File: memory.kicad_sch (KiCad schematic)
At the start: 0 parts

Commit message: Gathering memory components
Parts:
- added IC5: S70KL1282GABHV020, BGA24C100P5X5_600X800X100, symbol SamacSys_Parts:S70KL1282GABHV020
- added IC6: MT25QU02GCBB8E12-0AAT, BGA24C100P5X5_600X800X120, symbol SamacSys_Parts:MT25QU02GCBB8E12-0AAT
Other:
- note added: "HyperRAM (Fast DRAM)"
- note added: "NOR FLASH"
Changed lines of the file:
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@@
 (kicad_sch (version 20230121) (generator eeschema)
-  (paper "A4")
+  (paper "A5")
   (title_block
     (title "Memory")
   )
+  (text "HyperRAM (Fast DRAM)" (at 57.15 62.23 0)
+    (effects (font (size 1.27 1.27)) (justify left bottom))
+  )
+  (text "NOR FLASH" (at 140.97 77.47 0)
+    (effects (font (size 1.27 1.27)) (justify left bottom))
+  )
+  (symbol (lib_id "SamacSys_Parts:MT25QU02GCBB8E12-0AAT") (at 127 44.45 0) (unit 1)
+    (in_bom yes) (on_board yes) (dnp no) (fields_autoplaced)
+    (property "Reference" "IC6" (at 146.05 36.83 0)
+      (effects (font (size 1.27 1.27)))
+    )
+    (property "Value" "MT25QU02GCBB8E12-0AAT" (at 146.05 39.37 0)
+      (effects (font (size 1.27 1.27)))
+    )
+    (property "Footprint" "BGA24C100P5X5_600X800X120" (at 161.29 139.37 0)
+      (effects (font (size 1.27 1.27)) (justify left top) hide)
+    )
+    (property "Datasheet" "https://datasheet.datasheetarchive.com/originals/distributors/DKDS42/DSANUWW0045439.pdf" (at 161.29 239.37 0)
+      (effects (font (size 1.27 1.27)) (justify left top) hide)
+    )
+    (property "Height" "1.2" (at 161.29 439.37 0)
+      (effects (font (size 1.27 1.27)) (justify left top) hide)
+    )
+    (property "Mouser Part Number" "340-336522-TRAY" (at 161.29 539.37 0)
+      (effects (font (size 1.27 1.27)) (justify left top) hide)
+    )
+    (property "Mouser Price/Stock" "https://www.mouser.co.uk/ProductDetail/Micron/MT25QU02GCBB8E12-0AAT?qs=rrS6PyfT74d7p8mPaOod1Q%3D%3D" (at 161.29 639.37 0)
+      (effects (font (size 1.27 1.27)) (justify left top) hide)
+    )
+    (property "Manufacturer_Name" "Micron" (at 161.29 739.37 0)
+      (effects (font (size 1.27 1.27)) (justify left top) hide)
+    )
+    (property "Manufacturer_Part_Number" "MT25QU02GCBB8E12-0AAT" (at 161.29 839.37 0)
+      (effects (font (size 1.27 1.27)) (justify left top) hide)
+    )
+    (pin "E3")
+    (pin "C3")
+    (pin "B1")
+    (pin "C4")
+    (pin "C5")
+    (pin "D5")
+    (pin "B4")
+    (pin "B3")
+    (pin "E5")
+    (pin "E2")
+    (pin "A4")
+    (pin "D2")
+    (pin "B5")
+    (pin "A5")
+    (pin "A3")
+    (pin "B2")
+    (pin "D3")
+    (pin "E4")
+    (pin "C1")
+    (pin "C2")
+    (pin "D1")
+    (pin "A2")
+    (pin "E1")
+    (pin "D4")
+    (instances
+      (project "drone"
+        (path "/d34d8324-c983-4098-8d7e-5c2fbd34794d/4100cf90-4d91-4a61-8724-d501936d5e21"
+          (reference "IC6") (unit 1)
+        )
+      )
+    )
+  )
+  (symbol (lib_id "SamacSys_Parts:S70KL1282GABHV020") (at 50.8 29.21 0) (unit 1)
+    (in_bom yes) (on_board yes) (dnp no) (fields_autoplaced)
+    (property "Reference" "IC5" (at 67.31 21.59 0)
+      (effects (font (size 1.27 1.27)))
+    )
+    (property "Value" "S70KL1282GABHV020" (at 67.31 24.13 0)
+      (effects (font (size 1.27 1.27)))
+    )
+    (property "Footprint" "BGA24C100P5X5_600X800X100" (at 80.01 124.13 0)
+      (effects (font (size 1.27 1.27)) (justify left top) hide)
+    )
+    (property "Datasheet" "https://www.cypress.com/file/501841/download" (at 80.01 224.13 0)
+      (effects (font (size 1.27 1.27)) (justify left top) hide)
+    )
+    (property "Height" "1" (at 80.01 424.13 0)
+      (effects (font (size 1.27 1.27)) (justify left top) hide)
+    )
+    (property "Mouser Part Number" "727-S70KL1282GABHV2" (at 80.01 524.13 0)
+      (effects (font (size 1.27 1.27)) (justify left top) hide)
+    )
+    (property "Mouser Price/Stock" "https://www.mouser.co.uk/ProductDetail/Infineon-Technologies/S70KL1282GABHV020?qs=sPbYRqrBIVnZUdfTED8OOQ%3D%3D" (at 80.01 624.13 0)
+      (effects (font (size 1.27 1.27)) (justify left top) hide)
+    )
+    (property "Manufacturer_Name" "Infineon" (at 80.01 724.13 0)
+      (effects (font (size 1.27 1.27)) (justify left top) hide)
+    )
+    (property "Manufacturer_Part_Number" "S70KL1282GABHV020" (at 80.01 824.13 0)
+      (effects (font (size 1.27 1.27)) (justify left top) hide)
+    )
+    (pin "E4")
+    (pin "B5")
+    (pin "A2")
+    (pin "C5")
+    (pin "E5")
+    (pin "E2")
+    (pin "C2")
+    (pin "D2")
+    (pin "A5")
+    (pin "E1")
+    (pin "D5")
+    (pin "B3")
+    (pin "D3")
+    (pin "B4")
+    (pin "C4")
+    (pin "B2")
+    (pin "D1")
+    (pin "C1")
+    (pin "C3")
+    (pin "A4")
+    (pin "E3")
+    (pin "A3")
+    (pin "B1")
+    (pin "D4")
+    (instances
+      (project "drone"
+        (path "/d34d8324-c983-4098-8d7e-5c2fbd34794d/4100cf90-4d91-4a61-8724-d501936d5e21"
+          (reference "IC5") (unit 1)
+        )
+      )
+    )
+  )
 )

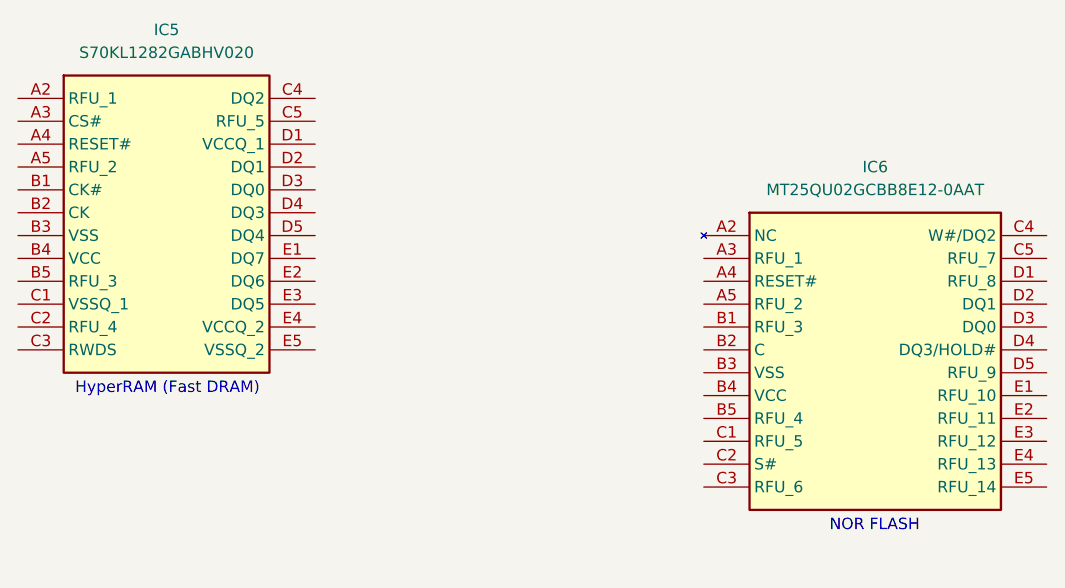
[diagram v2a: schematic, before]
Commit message: Exchanged flash for same one as on the gatemate dev board
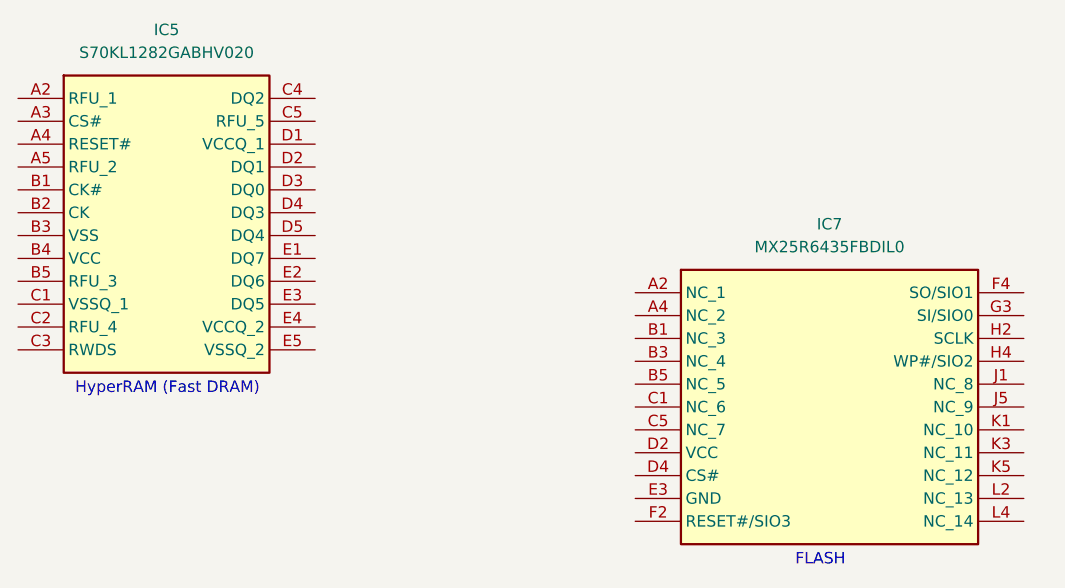
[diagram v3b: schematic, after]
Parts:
- removed IC6: MT25QU02GCBB8E12-0AAT, BGA24C100P5X5_600X800X120, symbol SamacSys_Parts:MT25QU02GCBB8E12-0AAT
- added IC7: MX25R6435FBDIL0, MX25R6435FBDIL0, symbol SamacSys_Parts:MX25R6435FBDIL0
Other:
- note added: "FLASH"
- note removed: "NOR FLASH"
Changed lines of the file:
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@@
 		)
 	)
-	(text "NOR FLASH"
+	(text "FLASH"
 		(exclude_from_sim no)
-		(at 140.97 77.47 0)
+		(at 137.16 81.28 0)
 		(effects
 			(font
@@
 			)
 			(justify left bottom)
-		)
-	)
-	(symbol
-		(lib_id "SamacSys_Parts:MT25QU02GCBB8E12-0AAT")
-		(at 127 44.45 0)
-		(unit 1)
-		(exclude_from_sim no)
-		(in_bom yes)
-		(on_board yes)
-		(dnp no)
-		(fields_autoplaced yes)
-		(property "Reference" "IC6"
-			(at 146.05 36.83 0)
-			(effects
-				(font
-					(size 1.27 1.27)
-				)
-			)
-		)
-		(property "Value" "MT25QU02GCBB8E12-0AAT"
-			(at 146.05 39.37 0)
-			(effects
-				(font
-					(size 1.27 1.27)
-				)
-			)
-		)
-		(property "Footprint" "BGA24C100P5X5_600X800X120"
-			(at 161.29 139.37 0)
-			(effects
-				(font
-					(size 1.27 1.27)
-				)
-				(justify left top)
-				(hide yes)
-			)
-		)
-		(property "Datasheet" "https://datasheet.datasheetarchive.com/originals/distributors/DKDS42/DSANUWW0045439.pdf"
-			(at 161.29 239.37 0)
-			(effects
-				(font
-					(size 1.27 1.27)
-				)
-				(justify left top)
-				(hide yes)
-			)
-		)
-		(property "Description" ""
-			(at 127 44.45 0)
-			(effects
-				(font
-					(size 1.27 1.27)
-				)
-				(hide yes)
-			)
-		)
-		(property "Height" "1.2"
-			(at 161.29 439.37 0)
-			(effects
-				(font
-					(size 1.27 1.27)
-				)
-				(justify left top)
-				(hide yes)
-			)
-		)
-		(property "Mouser Part Number" "340-336522-TRAY"
-			(at 161.29 539.37 0)
-			(effects
-				(font
-					(size 1.27 1.27)
-				)
-				(justify left top)
-				(hide yes)
-			)
-		)
-		(property "Mouser Price/Stock" "https://www.mouser.co.uk/ProductDetail/Micron/MT25QU02GCBB8E12-0AAT?qs=rrS6PyfT74d7p8mPaOod1Q%3D%3D"
-			(at 161.29 639.37 0)
-			(effects
-				(font
-					(size 1.27 1.27)
-				)
-				(justify left top)
-				(hide yes)
-			)
-		)
-		(property "Manufacturer_Name" "Micron"
-			(at 161.29 739.37 0)
-			(effects
-				(font
-					(size 1.27 1.27)
-				)
-				(justify left top)
-				(hide yes)
-			)
-		)
-		(property "Manufacturer_Part_Number" "MT25QU02GCBB8E12-0AAT"
-			(at 161.29 839.37 0)
-			(effects
-				(font
-					(size 1.27 1.27)
-				)
-				(justify left top)
-				(hide yes)
-			)
-		)
-		(pin "E3"
-		)
-		(pin "C3"
-		)
-		(pin "B1"
-		)
-		(pin "C4"
-		)
-		(pin "C5"
-		)
-		(pin "D5"
-		)
-		(pin "B4"
-		)
-		(pin "B3"
-		)
-		(pin "E5"
-		)
-		(pin "E2"
-		)
-		(pin "A4"
-		)
-		(pin "D2"
-		)
-		(pin "B5"
-		)
-		(pin "A5"
-		)
-		(pin "A3"
-		)
-		(pin "B2"
-		)
-		(pin "D3"
-		)
-		(pin "E4"
-		)
-		(pin "C1"
-		)
-		(pin "C2"
-		)
-		(pin "D1"
-		)
-		(pin "A2"
-		)
-		(pin "E1"
-		)
-		(pin "D4"
-		)
-		(instances
-			(project "drone"
-				(path "/d34d8324-c983-4098-8d7e-5c2fbd34794d/4100cf90-4d91-4a61-8724-d501936d5e21"
-					(reference "IC6")
-					(unit 1)
-				)
-			)
 		)
 	)
@@
 					(unit 1)
 				)
+			)
+		)
+	)
+	(symbol
+		(lib_id "SamacSys_Parts:MX25R6435FBDIL0")
+		(at 119.38 50.8 0)
+		(unit 1)
+		(exclude_from_sim no)
+		(in_bom yes)
+		(on_board yes)
+		(dnp no)
+		(fields_autoplaced yes)
+		(property "Reference" "IC7"
+			(at 140.97 43.18 0)
+			(effects
+				(font
+					(size 1.27 1.27)
+				)
+			)
+		)
+		(property "Value" "MX25R6435FBDIL0"
+			(at 140.97 45.72 0)
+			(effects
+				(font
+					(size 1.27 1.27)
+				)
+			)
+		)
+		(property "Footprint" "MX25R6435FBDIL0"
+			(at 158.75 145.72 0)
+			(effects
+				(font
+					(size 1.27 1.27)
+				)
+				(justify left top)
+				(hide yes)
+			)
+		)
+		(property "Datasheet" "https://datasheet.datasheetarchive.com/originals/distributors/DKDS-14/274584.pdf"
+			(at 158.75 245.72 0)
+			(effects
+				(font
+					(size 1.27 1.27)
+				)
+				(justify left top)
+				(hide yes)
+			)
+		)
+		(property "Description" "IC FLASH 64MBIT"
+			(at 119.38 50.8 0)
+			(effects
+				(font
+					(size 1.27 1.27)
+				)
+				(hide yes)
+			)
+		)
+		(property "Height" "0.52"
+			(at 158.75 445.72 0)
+			(effects
+				(font
+					(size 1.27 1.27)
+				)
+				(justify left top)
+				(hide yes)
+			)
+		)
+		(property "Manufacturer_Name" "Macronix"
+			(at 158.75 545.72 0)
+			(effects
+				(font
+					(size 1.27 1.27)
+				)
+				(justify left top)
+				(hide yes)
+			)
+		)
+		(property "Manufacturer_Part_Number" "MX25R6435FBDIL0"
+			(at 158.75 645.72 0)
+			(effects
+				(font
+					(size 1.27 1.27)
+				)
+				(justify left top)
+				(hide yes)
+			)
+		)
+		(property "Mouser Part Number" ""
+			(at 158.75 745.72 0)
+			(effects
+				(font
+					(size 1.27 1.27)
+				)
+				(justify left top)
+				(hide yes)
+			)
+		)
+		(property "Mouser Price/Stock" ""
+			(at 158.75 845.72 0)
+			(effects
+				(font
+					(size 1.27 1.27)
+				)
+				(justify left top)
+				(hide yes)
+			)
+		)
+		(property "Arrow Part Number" "MX25R6435FBDIL0"
+			(at 158.75 945.72 0)
+			(effects
+				(font
+					(size 1.27 1.27)
+				)
+				(justify left top)
+				(hide yes)
+			)
+		)
+		(property "Arrow Price/Stock" "https://www.arrow.com/en/products/mx25r6435fbdil0/macronix-international?region=nac"
+			(at 158.75 1045.72 0)
+			(effects
+				(font
+					(size 1.27 1.27)
+				)
+				(justify left top)
+				(hide yes)
+			)
+		)
+		(pin "A4"
+		)
+		(pin "E3"
+		)
+		(pin "K3"
+		)
+		(pin "B1"
+		)
+		(pin "D4"
+		)
+		(pin "H4"
+		)
+		(pin "D2"
+		)
+		(pin "K5"
+		)
+		(pin "H2"
+		)
+		(pin "L4"
+		)
+		(pin "F2"
+		)
+		(pin "K1"
+		)
+		(pin "B3"
+		)
+		(pin "L2"
+		)
+		(pin "C1"
+		)
+		(pin "B5"
+		)
+		(pin "F4"
+		)
+		(pin "G3"
+		)
+		(pin "J1"
+		)
+		(pin "J5"
+		)
+		(pin "C5"
+		)
+		(pin "A2"
+		)
+		(instances
+			(project ""
+				(path "/d34d8324-c983-4098-8d7e-5c2fbd34794d/4100cf90-4d91-4a61-8724-d501936d5e21"
+					(reference "IC7")
+					(unit 1)
+				)

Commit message: Added programmer for FPGA
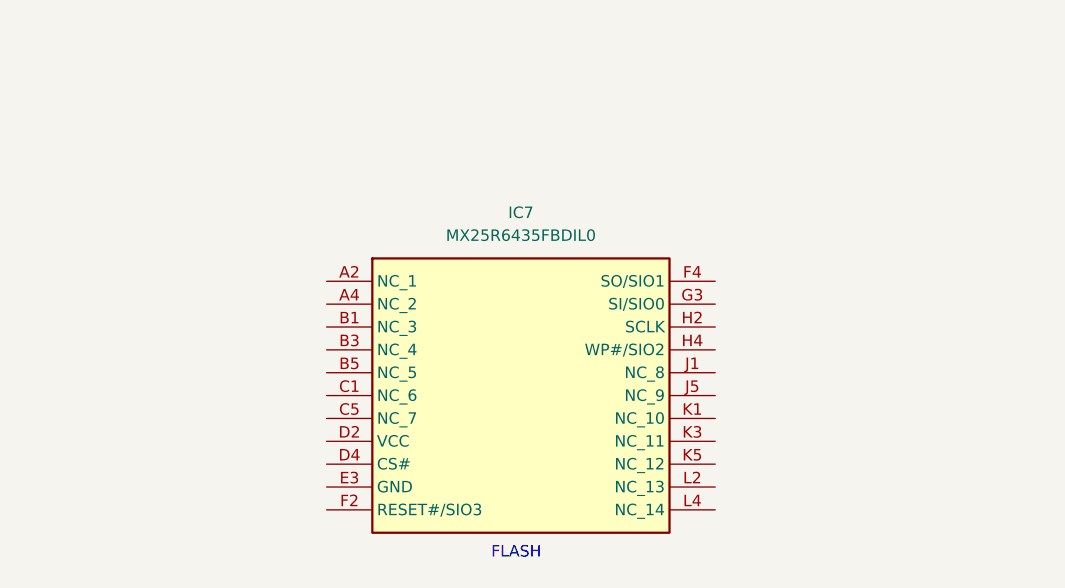
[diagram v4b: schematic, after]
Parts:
- removed IC5: S70KL1282GABHV020, BGA24C100P5X5_600X800X100, symbol SamacSys_Parts:S70KL1282GABHV020
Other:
- note removed: "HyperRAM (Fast DRAM)"
- moved on the sheet: IC7
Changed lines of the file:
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@@
 		(title "Memory")
-	)
-	(text "HyperRAM (Fast DRAM)"
-		(exclude_from_sim no)
-		(at 57.15 62.23 0)
-		(effects
-			(font
-				(size 1.27 1.27)
-			)
-			(justify left bottom)
-		)
 	)
 	(text "FLASH"
 		(exclude_from_sim no)
-		(at 137.16 81.28 0)
+		(at 103.378 80.518 0)
 		(effects
 			(font
@@
 	)
 	(symbol
-		(lib_id "SamacSys_Parts:S70KL1282GABHV020")
-		(at 50.8 29.21 0)
-		(unit 1)
-		(exclude_from_sim no)
-		(in_bom yes)
-		(on_board yes)
-		(dnp no)
-		(fields_autoplaced yes)
-		(property "Reference" "IC5"
-			(at 67.31 21.59 0)
-			(effects
-				(font
-					(size 1.27 1.27)
-				)
-			)
-		)
-		(property "Value" "S70KL1282GABHV020"
-			(at 67.31 24.13 0)
-			(effects
-				(font
-					(size 1.27 1.27)
-				)
-			)
-		)
-		(property "Footprint" "BGA24C100P5X5_600X800X100"
-			(at 80.01 124.13 0)
-			(effects
-				(font
-					(size 1.27 1.27)
-				)
-				(justify left top)
-				(hide yes)
-			)
-		)
-		(property "Datasheet" "https://www.cypress.com/file/501841/download"
-			(at 80.01 224.13 0)
-			(effects
-				(font
-					(size 1.27 1.27)
-				)
-				(justify left top)
-				(hide yes)
-			)
-		)
-		(property "Description" ""
-			(at 50.8 29.21 0)
-			(effects
-				(font
-					(size 1.27 1.27)
-				)
-				(hide yes)
-			)
-		)
-		(property "Height" "1"
-			(at 80.01 424.13 0)
-			(effects
-				(font
-					(size 1.27 1.27)
-				)
-				(justify left top)
-				(hide yes)
-			)
-		)
-		(property "Mouser Part Number" "727-S70KL1282GABHV2"
-			(at 80.01 524.13 0)
-			(effects
-				(font
-					(size 1.27 1.27)
-				)
-				(justify left top)
-				(hide yes)
-			)
-		)
-		(property "Mouser Price/Stock" "https://www.mouser.co.uk/ProductDetail/Infineon-Technologies/S70KL1282GABHV020?qs=sPbYRqrBIVnZUdfTED8OOQ%3D%3D"
-			(at 80.01 624.13 0)
-			(effects
-				(font
-					(size 1.27 1.27)
-				)
-				(justify left top)
-				(hide yes)
-			)
-		)
-		(property "Manufacturer_Name" "Infineon"
-			(at 80.01 724.13 0)
-			(effects
-				(font
-					(size 1.27 1.27)
-				)
-				(justify left top)
-				(hide yes)
-			)
-		)
-		(property "Manufacturer_Part_Number" "S70KL1282GABHV020"
-			(at 80.01 824.13 0)
-			(effects
-				(font
-					(size 1.27 1.27)
-				)
-				(justify left top)
-				(hide yes)
-			)
-		)
-		(pin "E4"
-		)
-		(pin "B5"
-		)
-		(pin "A2"
-		)
-		(pin "C5"
-		)
-		(pin "E5"
-		)
-		(pin "E2"
-		)
-		(pin "C2"
-		)
-		(pin "D2"
-		)
-		(pin "A5"
-		)
-		(pin "E1"
-		)
-		(pin "D5"
-		)
-		(pin "B3"
-		)
-		(pin "D3"
-		)
-		(pin "B4"
-		)
-		(pin "C4"
-		)
-		(pin "B2"
-		)
-		(pin "D1"
-		)
-		(pin "C1"
-		)
-		(pin "C3"
-		)
-		(pin "A4"
-		)
-		(pin "E3"
-		)
-		(pin "A3"
-		)
-		(pin "B1"
-		)
-		(pin "D4"
-		)
-		(instances
-			(project "drone"
-				(path "/d34d8324-c983-4098-8d7e-5c2fbd34794d/4100cf90-4d91-4a61-8724-d501936d5e21"
-					(reference "IC5")
-					(unit 1)
-				)
-			)
-		)
-	)
-	(symbol
 		(lib_id "SamacSys_Parts:MX25R6435FBDIL0")
-		(at 119.38 50.8 0)
+		(at 85.09 49.53 0)
 		(unit 1)
 		(exclude_from_sim no)
@@
 		(fields_autoplaced yes)
 		(property "Reference" "IC7"
-			(at 140.97 43.18 0)
+			(at 106.68 41.91 0)
 			(effects
 				(font
@@
 		)
 		(property "Value" "MX25R6435FBDIL0"
-			(at 140.97 45.72 0)
+			(at 106.68 44.45 0)
 			(effects
 				(font
@@
 		)
 		(property "Footprint" "MX25R6435FBDIL0"
-			(at 158.75 145.72 0)
+			(at 124.46 144.45 0)
 			(effects
 				(font
@@
 		)
 		(property "Datasheet" "https://datasheet.datasheetarchive.com/originals/distributors/DKDS-14/274584.pdf"
-			(at 158.75 245.72 0)
+			(at 124.46 244.45 0)
 			(effects
 				(font
@@
 		)
 		(property "Description" "IC FLASH 64MBIT"
-			(at 119.38 50.8 0)
+			(at 85.09 49.53 0)
 			(effects
 				(font
@@
 		)
 		(property "Height" "0.52"
-			(at 158.75 445.72 0)
+			(at 124.46 444.45 0)
 			(effects
 				(font
@@
 		)
 		(property "Manufacturer_Name" "Macronix"
-			(at 158.75 545.72 0)
+			(at 124.46 544.45 0)
 			(effects
 				(font
@@
 		)
 		(property "Manufacturer_Part_Number" "MX25R6435FBDIL0"
-			(at 158.75 645.72 0)
+			(at 124.46 644.45 0)
 			(effects
 				(font
@@
 		)
 		(property "Mouser Part Number" ""
-			(at 158.75 745.72 0)
+			(at 124.46 744.45 0)
 			(effects
 				(font
@@
 		)
 		(property "Mouser Price/Stock" ""
-			(at 158.75 845.72 0)
+			(at 124.46 844.45 0)
 			(effects
 				(font
@@
 		)
 		(property "Arrow Part Number" "MX25R6435FBDIL0"
-			(at 158.75 945.72 0)
+			(at 124.46 944.45 0)
 			(effects
 				(font
@@
 		)
 		(property "Arrow Price/Stock" "https://www.arrow.com/en/products/mx25r6435fbdil0/macronix-international?region=nac"
-			(at 158.75 1045.72 0)
+			(at 124.46 1044.45 0)
 			(effects
 				(font
